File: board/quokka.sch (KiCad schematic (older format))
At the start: 0 parts

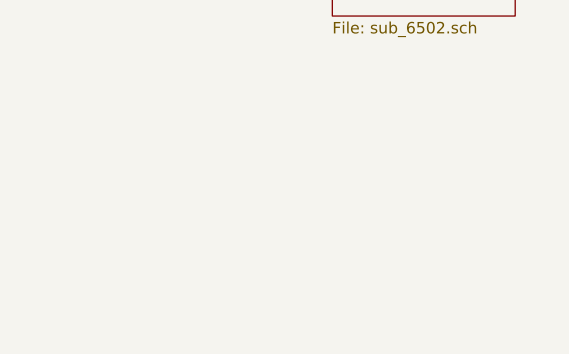
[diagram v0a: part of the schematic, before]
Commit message: Cleaned up silkscreen designators
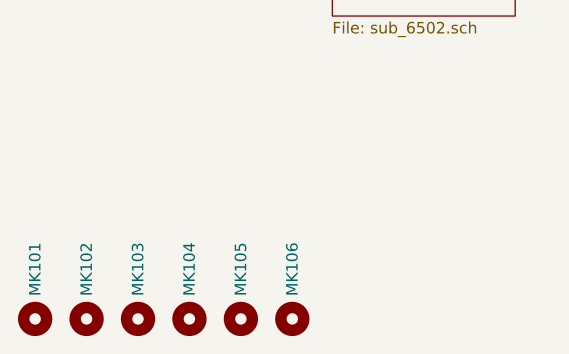
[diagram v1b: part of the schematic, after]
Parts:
- added MK101, MK102, MK103, MK104, MK105, MK106: Mounting_Hole, MountingHole:MountingHole_4.5mm, symbol Mechanical:Mounting_Hole
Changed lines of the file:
@@
 Wire Wire Line
 	8350 3625 8625 3625
+$Comp
+L Mechanical:Mounting_Hole MK101
+U 1 1 5AB418EE
+P 950 7650
+F 0 "MK101" V 950 7750 50  0000 L CNN
+F 1 "Mounting_Hole" H 1050 7605 50  0001 L CNN
+F 2 "MountingHole:MountingHole_4.5mm" H 950 7650 50  0001 C CNN
+F 3 "" H 950 7650 50  0001 C CNN
+	1    950  7650
+	1    0    0    -1
+$EndComp
+$Comp
+L Mechanical:Mounting_Hole MK102
+U 1 1 5AB41A93
+P 1175 7650
+F 0 "MK102" V 1175 7750 50  0000 L CNN
+F 1 "Mounting_Hole" H 1275 7605 50  0001 L CNN
+F 2 "MountingHole:MountingHole_4.5mm" H 1175 7650 50  0001 C CNN
+F 3 "" H 1175 7650 50  0001 C CNN
+	1    1175 7650
+	1    0    0    -1
+$EndComp
+$Comp
+L Mechanical:Mounting_Hole MK104
+U 1 1 5AB44047
+P 1625 7650
+F 0 "MK104" V 1625 7750 50  0000 L CNN
+F 1 "Mounting_Hole" H 1725 7605 50  0001 L CNN
+F 2 "MountingHole:MountingHole_4.5mm" H 1625 7650 50  0001 C CNN
+F 3 "" H 1625 7650 50  0001 C CNN
+	1    1625 7650
+	1    0    0    -1
+$EndComp
+$Comp
+L Mechanical:Mounting_Hole MK103
+U 1 1 5AB44041
+P 1400 7650
+F 0 "MK103" V 1400 7750 50  0000 L CNN
+F 1 "Mounting_Hole" H 1500 7605 50  0001 L CNN
+F 2 "MountingHole:MountingHole_4.5mm" H 1400 7650 50  0001 C CNN
+F 3 "" H 1400 7650 50  0001 C CNN
+	1    1400 7650
+	1    0    0    -1
+$EndComp
+$Comp
+L Mechanical:Mounting_Hole MK106
+U 1 1 5AB48BB3
+P 2075 7650
+F 0 "MK106" V 2075 7750 50  0000 L CNN
+F 1 "Mounting_Hole" H 2175 7605 50  0001 L CNN
+F 2 "MountingHole:MountingHole_4.5mm" H 2075 7650 50  0001 C CNN
+F 3 "" H 2075 7650 50  0001 C CNN
+	1    2075 7650
+	1    0    0    -1
+$EndComp
+$Comp
+L Mechanical:Mounting_Hole MK105
+U 1 1 5AB48BB9
+P 1850 7650
+F 0 "MK105" V 1850 7750 50  0000 L CNN
+F 1 "Mounting_Hole" H 1950 7605 50  0001 L CNN
+F 2 "MountingHole:MountingHole_4.5mm" H 1850 7650 50  0001 C CNN
+F 3 "" H 1850 7650 50  0001 C CNN
+	1    1850 7650
+	1    0    0    -1
+$EndComp
 $EndSCHEMATC

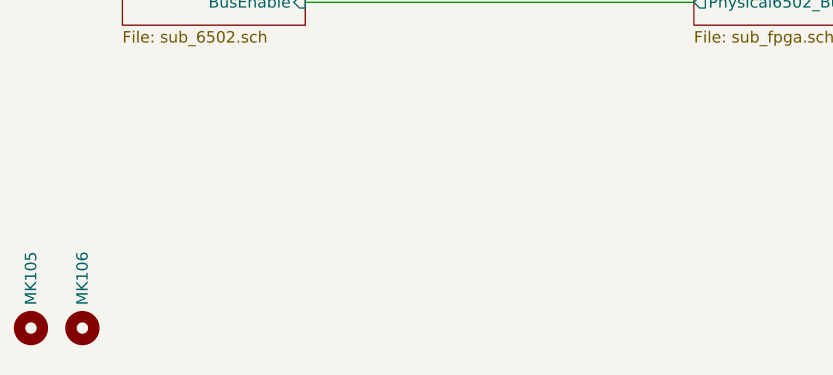
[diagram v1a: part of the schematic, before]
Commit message: Added fids, made PDF
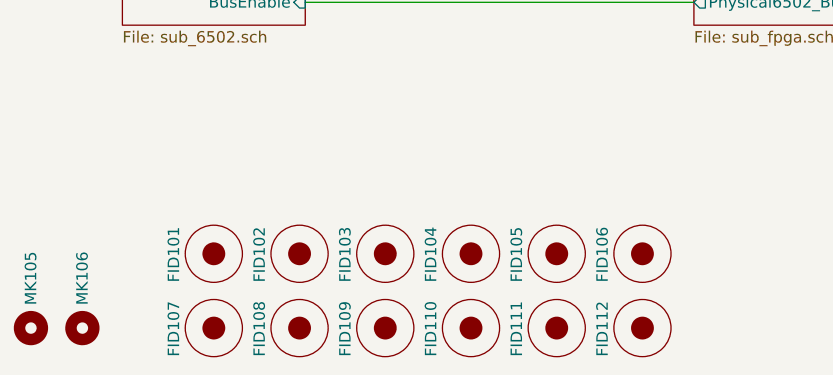
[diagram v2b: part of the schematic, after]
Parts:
- added FID101, FID102, FID103, FID107, FID108, FID109, FID110, FID111, FID112: Fiducial, Fiducial:Fiducial_1mm_Dia_2.54mm_Outer_CopperTop, symbol quokka:Fiducial
- added FID104, FID105, FID106: Fiducial, Fiducial:Fiducial_1mm_Dia_2.54mm_Outer_CopperBottom, symbol quokka:Fiducial
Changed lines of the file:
@@
+	1    0    0    -1
+$EndComp
+$Comp
+L quokka:Fiducial FID101
+U 1 1 5AB5F301
+P 2650 7325
+F 0 "FID101" V 2475 7200 50  0000 L CNN
+F 1 "Fiducial" H 2650 7450 50  0001 C CNN
+F 2 "Fiducial:Fiducial_1mm_Dia_2.54mm_Outer_CopperTop" H 2650 7325 50  0001 C CNN
+F 3 "" H 2650 7325 50  0001 C CNN
+	1    2650 7325
+	1    0    0    -1
+$EndComp
+$Comp
+L quokka:Fiducial FID102
+U 1 1 5AB5F428
+P 3025 7325
+F 0 "FID102" V 2850 7200 50  0000 L CNN
+F 1 "Fiducial" H 3025 7450 50  0001 C CNN
+F 2 "Fiducial:Fiducial_1mm_Dia_2.54mm_Outer_CopperTop" H 3025 7325 50  0001 C CNN
+F 3 "" H 3025 7325 50  0001 C CNN
+	1    3025 7325
+	1    0    0    -1
+$EndComp
+$Comp
+L quokka:Fiducial FID103
+U 1 1 5AB5F4F2
+P 3400 7325
+F 0 "FID103" V 3225 7200 50  0000 L CNN
+F 1 "Fiducial" H 3400 7450 50  0001 C CNN
+F 2 "Fiducial:Fiducial_1mm_Dia_2.54mm_Outer_CopperTop" H 3400 7325 50  0001 C CNN
+F 3 "" H 3400 7325 50  0001 C CNN
+	1    3400 7325
+	1    0    0    -1
+$EndComp
+$Comp
+L quokka:Fiducial FID104
+U 1 1 5AB5F4F8
+P 3775 7325
+F 0 "FID104" V 3600 7200 50  0000 L CNN
+F 1 "Fiducial" H 3775 7450 50  0001 C CNN
+F 2 "Fiducial:Fiducial_1mm_Dia_2.54mm_Outer_CopperBottom" H 3775 7325 50  0001 C CNN
+F 3 "" H 3775 7325 50  0001 C CNN
+	1    3775 7325
+	1    0    0    -1
+$EndComp
+$Comp
+L quokka:Fiducial FID105
+U 1 1 5AB61C6E
+P 4150 7325
+F 0 "FID105" V 3975 7200 50  0000 L CNN
+F 1 "Fiducial" H 4150 7450 50  0001 C CNN
+F 2 "Fiducial:Fiducial_1mm_Dia_2.54mm_Outer_CopperBottom" H 4150 7325 50  0001 C CNN
+F 3 "" H 4150 7325 50  0001 C CNN
+	1    4150 7325
+	1    0    0    -1
+$EndComp
+$Comp
+L quokka:Fiducial FID106
+U 1 1 5AB61C74
+P 4525 7325
+F 0 "FID106" V 4350 7200 50  0000 L CNN
+F 1 "Fiducial" H 4525 7450 50  0001 C CNN
+F 2 "Fiducial:Fiducial_1mm_Dia_2.54mm_Outer_CopperBottom" H 4525 7325 50  0001 C CNN
+F 3 "" H 4525 7325 50  0001 C CNN
+	1    4525 7325
+	1    0    0    -1
+$EndComp
+$Comp
+L quokka:Fiducial FID107
+U 1 1 5AB8207D
+P 2650 7650
+F 0 "FID107" V 2475 7525 50  0000 L CNN
+F 1 "Fiducial" H 2650 7775 50  0001 C CNN
+F 2 "Fiducial:Fiducial_1mm_Dia_2.54mm_Outer_CopperTop" H 2650 7650 50  0001 C CNN
+F 3 "" H 2650 7650 50  0001 C CNN
+	1    2650 7650
+	1    0    0    -1
+$EndComp
+$Comp
+L quokka:Fiducial FID108
+U 1 1 5AB82083
+P 3025 7650
+F 0 "FID108" V 2850 7525 50  0000 L CNN
+F 1 "Fiducial" H 3025 7775 50  0001 C CNN
+F 2 "Fiducial:Fiducial_1mm_Dia_2.54mm_Outer_CopperTop" H 3025 7650 50  0001 C CNN
+F 3 "" H 3025 7650 50  0001 C CNN
+	1    3025 7650
+	1    0    0    -1
+$EndComp
+$Comp
+L quokka:Fiducial FID109
+U 1 1 5AB82089
+P 3400 7650
+F 0 "FID109" V 3225 7525 50  0000 L CNN
+F 1 "Fiducial" H 3400 7775 50  0001 C CNN
+F 2 "Fiducial:Fiducial_1mm_Dia_2.54mm_Outer_CopperTop" H 3400 7650 50  0001 C CNN
+F 3 "" H 3400 7650 50  0001 C CNN
+	1    3400 7650
+	1    0    0    -1
+$EndComp
+$Comp
+L quokka:Fiducial FID110
+U 1 1 5AB84731
+P 3775 7650
+F 0 "FID110" V 3600 7525 50  0000 L CNN
+F 1 "Fiducial" H 3775 7775 50  0001 C CNN
+F 2 "Fiducial:Fiducial_1mm_Dia_2.54mm_Outer_CopperTop" H 3775 7650 50  0001 C CNN
+F 3 "" H 3775 7650 50  0001 C CNN
+	1    3775 7650
+	1    0    0    -1
+$EndComp
+$Comp
+L quokka:Fiducial FID111
+U 1 1 5AB84737
+P 4150 7650
+F 0 "FID111" V 3975 7525 50  0000 L CNN
+F 1 "Fiducial" H 4150 7775 50  0001 C CNN
+F 2 "Fiducial:Fiducial_1mm_Dia_2.54mm_Outer_CopperTop" H 4150 7650 50  0001 C CNN
+F 3 "" H 4150 7650 50  0001 C CNN
+	1    4150 7650
+	1    0    0    -1
+$EndComp
+$Comp
+L quokka:Fiducial FID112
+U 1 1 5AB8473D
+P 4525 7650
+F 0 "FID112" V 4350 7525 50  0000 L CNN
+F 1 "Fiducial" H 4525 7775 50  0001 C CNN
+F 2 "Fiducial:Fiducial_1mm_Dia_2.54mm_Outer_CopperTop" H 4525 7650 50  0001 C CNN
+F 3 "" H 4525 7650 50  0001 C CNN
+	1    4525 7650
 	1    0    0    -1
 $EndComp
